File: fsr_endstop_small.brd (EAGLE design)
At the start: 27.9 x 30.5 mm, 33 parts, among them U1 ATTINY461

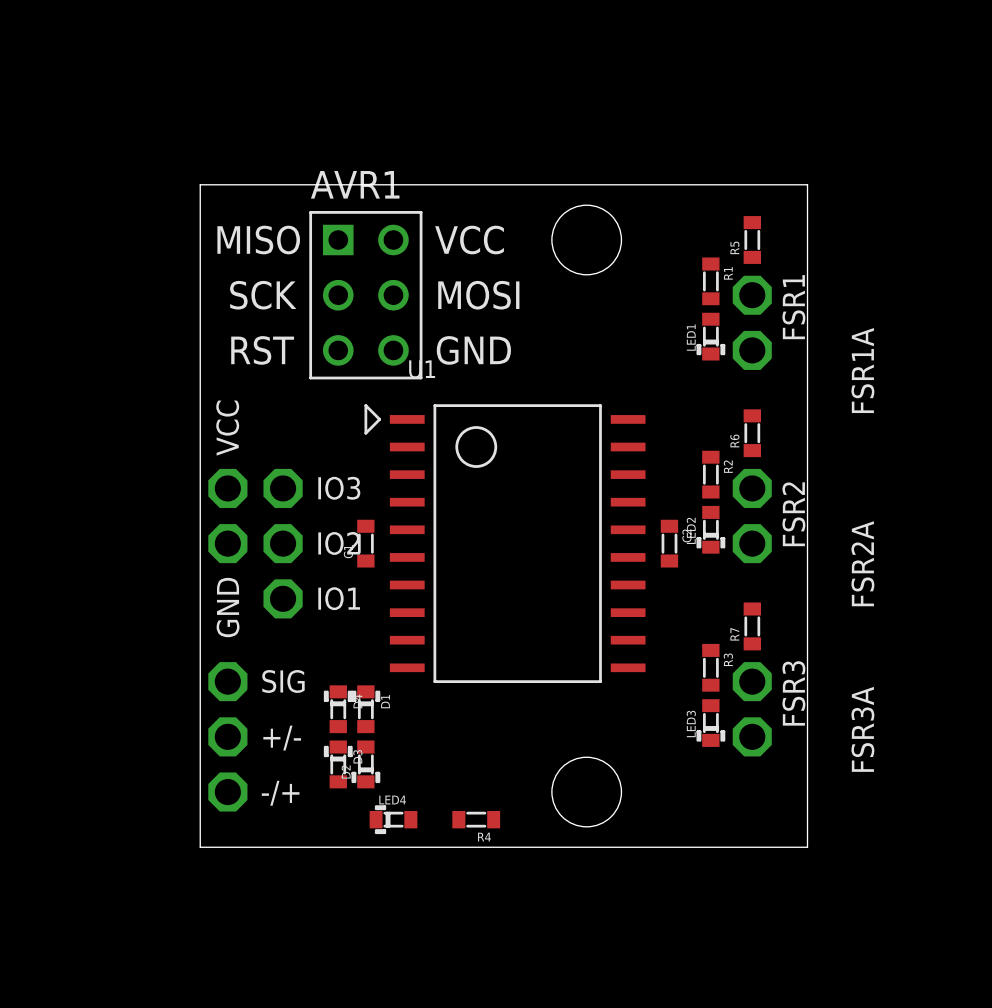
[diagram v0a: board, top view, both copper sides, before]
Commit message: Completed non-GND routing
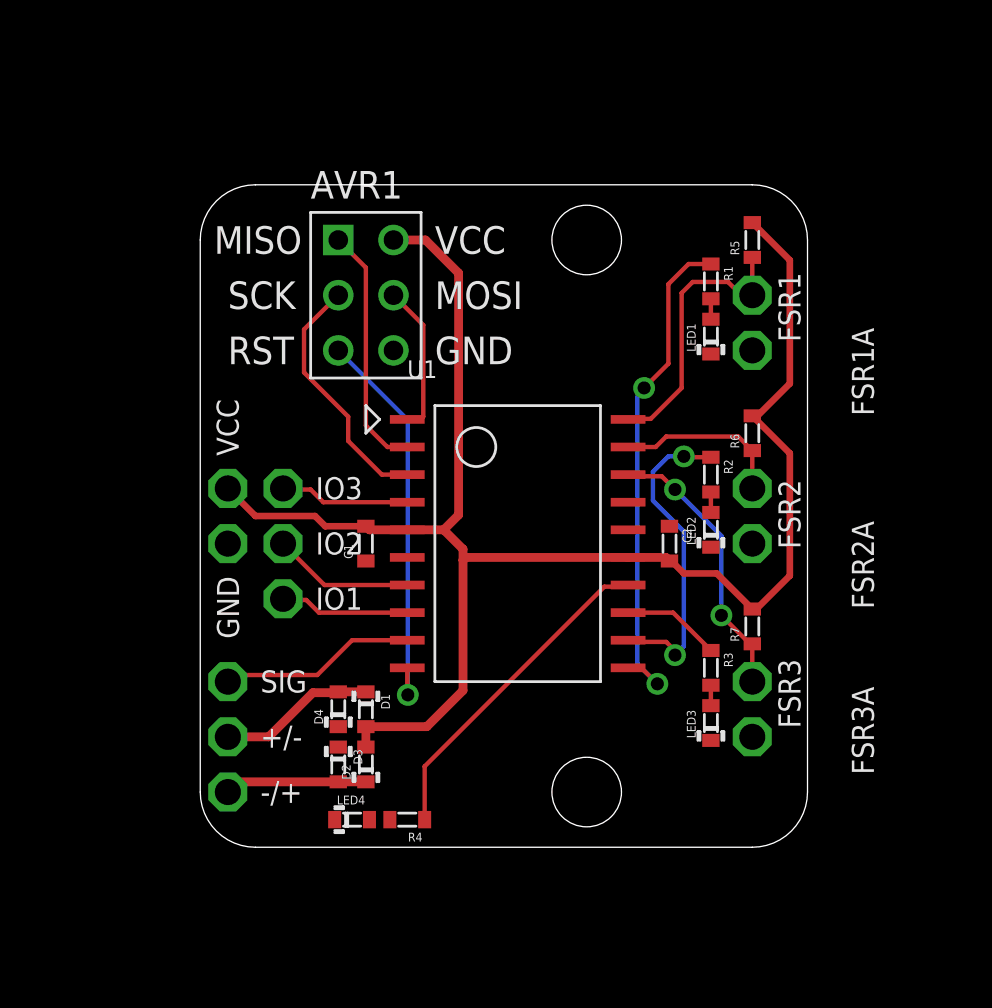
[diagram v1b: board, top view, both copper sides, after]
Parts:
- moved R4 3.17 mm to (22.2, 14.0)
- moved LED4 1.91 mm to (19.7, 14.0)
- turned D4 to 90 degrees
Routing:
- net V+: track 0.00 -> 75.5 mm
- net N$13: track 0.00 -> 23.4 mm, vias 0 -> 2
- net N$6: track 0.00 -> 18.4 mm, vias 0 -> 1
- net N$10: track 0.00 -> 15.3 mm
- net N$12: track 0.00 -> 14.7 mm, vias 0 -> 2
- net N$7: track 0.00 -> 12.9 mm
- net N$9: track 0.00 -> 12.8 mm, vias 0 -> 2
- net N$5: track 0.00 -> 11.6 mm
- net N$2: track 0.00 -> 11.4 mm
- net N$14: track 0.00 -> 9.04 mm
- net N$8: track 0.00 -> 7.92 mm
- net N$4: track 0.00 -> 7.21 mm
- net N$1: track 0.00 -> 6.95 mm
- net N$3: track 0.00 -> 6.54 mm
- net N$17: track 0.00 -> 6.50 mm
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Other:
- outline, holes or cut-outs redrawn

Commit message: Added ground plane, done with small version
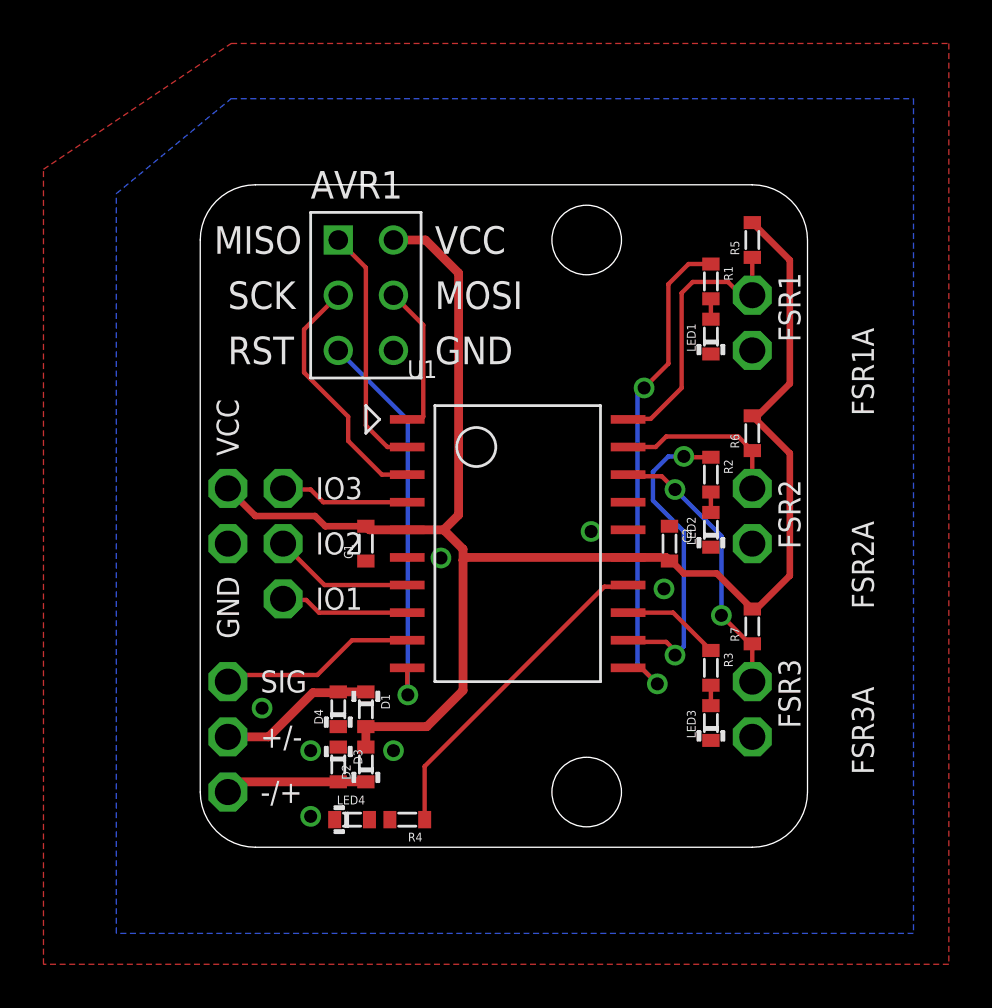
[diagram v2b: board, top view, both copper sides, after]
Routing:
- added copper zone on layer 1, net GND
- added copper zone on layer 16, net GND
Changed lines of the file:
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@@
 </class>
 </classes>
-<designrules name="default">
-<description language="de">&lt;b&gt;EAGLE Design Rules&lt;/b&gt;
-&lt;p&gt;
-Die Standard-Design-Rules sind so gewählt, dass sie für
-die meisten Anwendungen passen. Sollte ihre Platine
-besondere Anforderungen haben, treffen Sie die erforderlichen
-Einstellungen hier und speichern die Design Rules unter
-einem neuen Namen ab.</description>
+<designrules name="LaenPCBOrder">
 <description language="en">&lt;b&gt;EAGLE Design Rules&lt;/b&gt;
 &lt;p&gt;
@@
 design rules under a new name.</description>
 <param name="layerSetup" value="(1*16)"/>
-<param name="mtCopper" value="0.035mm 0.035mm 0.035mm 0.035mm 0.035mm 0.035mm 0.035mm 0.035mm 0.035mm 0.035mm 0.035mm 0.035mm 0.035mm 0.035mm 0.035mm 0.035mm"/>
-<param name="mtIsolate" value="1.5mm 0.15mm 0.2mm 0.15mm 0.2mm 0.15mm 0.2mm 0.15mm 0.2mm 0.15mm 0.2mm 0.15mm 0.2mm 0.15mm 0.2mm"/>
-<param name="mdWireWire" value="8mil"/>
-<param name="mdWirePad" value="8mil"/>
-<param name="mdWireVia" value="8mil"/>
-<param name="mdPadPad" value="8mil"/>
-<param name="mdPadVia" value="8mil"/>
-<param name="mdViaVia" value="8mil"/>
-<param name="mdSmdPad" value="8mil"/>
-<param name="mdSmdVia" value="8mil"/>
-<param name="mdSmdSmd" value="8mil"/>
+<param name="mtCopper" value="0.035559375mm 0.035559375mm 0.035559375mm 0.035559375mm 0.035559375mm 0.035559375mm 0.035559375mm 0.035559375mm 0.035559375mm 0.035559375mm 0.035559375mm 0.035559375mm 0.035559375mm 0.035559375mm 0.035559375mm 0.035559375mm"/>
+<param name="mtIsolate" value="1.501140625mm 0.149859375mm 0.200659375mm 0.149859375mm 0.200659375mm 0.149859375mm 0.200659375mm 0.149859375mm 0.200659375mm 0.149859375mm 0.200659375mm 0.149859375mm 0.200659375mm 0.149859375mm 0.200659375mm"/>
+<param name="mdWireWire" value="6mil"/>
+<param name="mdWirePad" value="6mil"/>
+<param name="mdWireVia" value="6mil"/>
+<param name="mdPadPad" value="6mil"/>
+<param name="mdPadVia" value="6mil"/>
+<param name="mdViaVia" value="6mil"/>
+<param name="mdSmdPad" value="6mil"/>
+<param name="mdSmdVia" value="6mil"/>
+<param name="mdSmdSmd" value="6mil"/>
 <param name="mdViaViaSameLayer" value="8mil"/>
 <param name="mnLayersViaInSmd" value="2"/>
-<param name="mdCopperDimension" value="40mil"/>
-<param name="mdDrill" value="8mil"/>
+<param name="mdCopperDimension" value="15mil"/>
+<param name="mdDrill" value="6mil"/>
 <param name="mdSmdStop" value="0mil"/>
-<param name="msWidth" value="10mil"/>
-<param name="msDrill" value="24mil"/>
-<param name="msMicroVia" value="9.99mm"/>
+<param name="msWidth" value="6mil"/>
+<param name="msDrill" value="13mil"/>
+<param name="msMicroVia" value="13mil"/>
 <param name="msBlindViaRatio" value="0.5"/>
 <param name="rvPadTop" value="0.25"/>
@@
 <param name="rvMicroViaOuter" value="0.25"/>
 <param name="rvMicroViaInner" value="0.25"/>
-<param name="rlMinPadTop" value="10mil"/>
+<param name="rlMinPadTop" value="7mil"/>
 <param name="rlMaxPadTop" value="20mil"/>
-<param name="rlMinPadInner" value="10mil"/>
+<param name="rlMinPadInner" value="7mil"/>
 <param name="rlMaxPadInner" value="20mil"/>
-<param name="rlMinPadBottom" value="10mil"/>
+<param name="rlMinPadBottom" value="7mil"/>
 <param name="rlMaxPadBottom" value="20mil"/>
-<param name="rlMinViaOuter" value="8mil"/>
+<param name="rlMinViaOuter" value="7mil"/>
 <param name="rlMaxViaOuter" value="20mil"/>
-<param name="rlMinViaInner" value="8mil"/>
+<param name="rlMinViaInner" value="7mil"/>
 <param name="rlMaxViaInner" value="20mil"/>
 <param name="rlMinMicroViaOuter" value="4mil"/>
@@
 <param name="mlMinCreamFrame" value="0mil"/>
 <param name="mlMaxCreamFrame" value="0mil"/>
-<param name="mlViaStopLimit" value="0mil"/>
+<param name="mlViaStopLimit" value="25mil"/>
 <param name="srRoundness" value="0"/>
 <param name="srMinRoundness" value="0mil"/>
@@
 <contactref element="LED4" pad="-"/>
 <contactref element="C2" pad="1"/>
-<wire x1="36.195" y1="35.395" x2="38.1" y2="35.56" width="0" layer="19" extent="1-1"/>
-<wire x1="34.29" y1="27.47" x2="36.195" y2="35.395" width="0" layer="19" extent="1-1"/>
-<wire x1="32.385" y1="27.305" x2="34.29" y2="27.47" width="0" layer="19" extent="1-1"/>
-<wire x1="36.195" y1="26.505" x2="34.29" y2="27.47" width="0" layer="19" extent="1-1"/>
-<wire x1="38.1" y1="26.67" x2="36.195" y2="26.505" width="0" layer="19" extent="1-1"/>
-<wire x1="38.1" y1="17.78" x2="38.1" y2="26.67" width="0" layer="19" extent="1-1"/>
-<wire x1="36.195" y1="17.615" x2="38.1" y2="17.78" width="0" layer="19" extent="1-1"/>
-<wire x1="22.225" y1="26.035" x2="32.385" y2="27.305" width="0" layer="19" extent="1-1"/>
-<wire x1="20.32" y1="25.87" x2="22.225" y2="26.035" width="0" layer="19" extent="1-1"/>
-<wire x1="19.05" y1="18.25" x2="20.32" y2="25.87" width="0" layer="19" extent="1-1"/>
-<wire x1="19.05" y1="17.31" x2="19.05" y2="18.25" width="0" layer="19" extent="1-1"/>
-<wire x1="18.885" y1="13.97" x2="19.05" y2="17.31" width="0" layer="19" extent="1-1"/>
-<wire x1="13.97" y1="26.67" x2="20.32" y2="25.87" width="0" layer="19" extent="1-1"/>
-<wire x1="21.59" y1="35.56" x2="22.225" y2="26.035" width="0" layer="19" extent="1-1"/>
+<polygon width="0.2032" layer="16" isolate="0.254">
+<vertex x="14.1224" y="47.1424"/>
+<vertex x="45.5168" y="47.1424"/>
+<vertex x="45.5168" y="8.7376"/>
+<vertex x="8.8392" y="8.7376"/>
+<vertex x="8.8392" y="42.7736"/>
+</polygon>
+<polygon width="0.2032" layer="1" isolate="0.254">
+<vertex x="14.1224" y="49.6824"/>
+<vertex x="47.1424" y="49.6824"/>
+<vertex x="47.1424" y="7.3152"/>
+<vertex x="5.4864" y="7.3152"/>
+<vertex x="5.4864" y="43.8912"/>
+</polygon>
+<via x="17.78" y="17.145" extent="1-16" drill="0.6"/>
+<via x="21.59" y="17.145" extent="1-16" drill="0.6"/>
+<via x="23.7744" y="26.0096" extent="1-16" drill="0.6"/>
+<via x="30.6832" y="27.2288" extent="1-16" drill="0.6"/>
+<via x="17.78" y="14.1224" extent="1-16" drill="0.6"/>
+<via x="34.036" y="24.5872" extent="1-16" drill="0.6"/>
+<via x="15.5448" y="19.1008" extent="1-16" drill="0.6"/>
 </signal>
 <signal name="N$1">
@@
 </signal>
 </signals>
+<errors>
+</errors>
 </board>
 </drawing>
